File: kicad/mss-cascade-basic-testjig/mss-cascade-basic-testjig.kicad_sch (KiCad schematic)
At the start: 101 parts, among them J1 PJ-202A, J11 Molex 0532610471, J12 Molex 0532610471, J2 SM04B-SRSS, J3 SM04B-SRSS, J4 SM04B-SRSS, J5 8P8C, J6 8P8C, Q1 ZXMS6004FF, Q10 ZXMS6004FF, Q11 ZXMS6004FF, Q12 ZXMS6004FF, Q2 ZXMS6004FF, Q3 ZXMS6004FF, Q4 ZXMS6004FF, Q5 ZXMS6004FF, Q6 ZXMS6004FF, Q7 ZXMS6004FF, Q8 ZXMS6004FF, Q9 ZXMS6004FF, SW1 FSM4JSMATR, SW2 FSM4JSMATR, U1 AP7381-50, U11 PCA9555PW, U2 DRV8872DDA, U3 74HC4049, U4 INA219AxD, U5 ProMicro

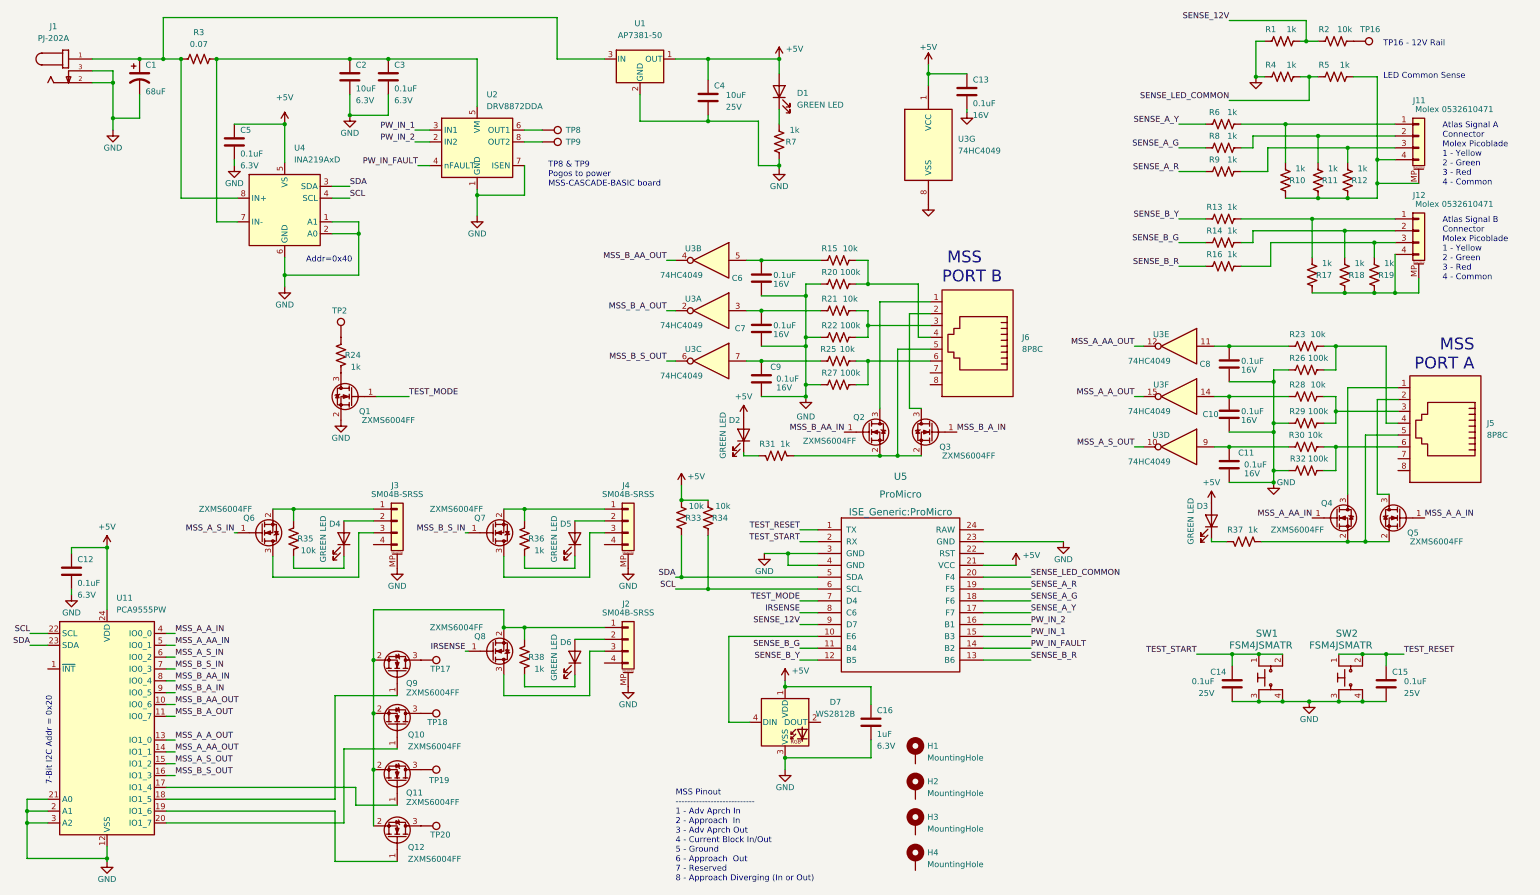
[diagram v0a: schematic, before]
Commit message: Fix issues with wire naming
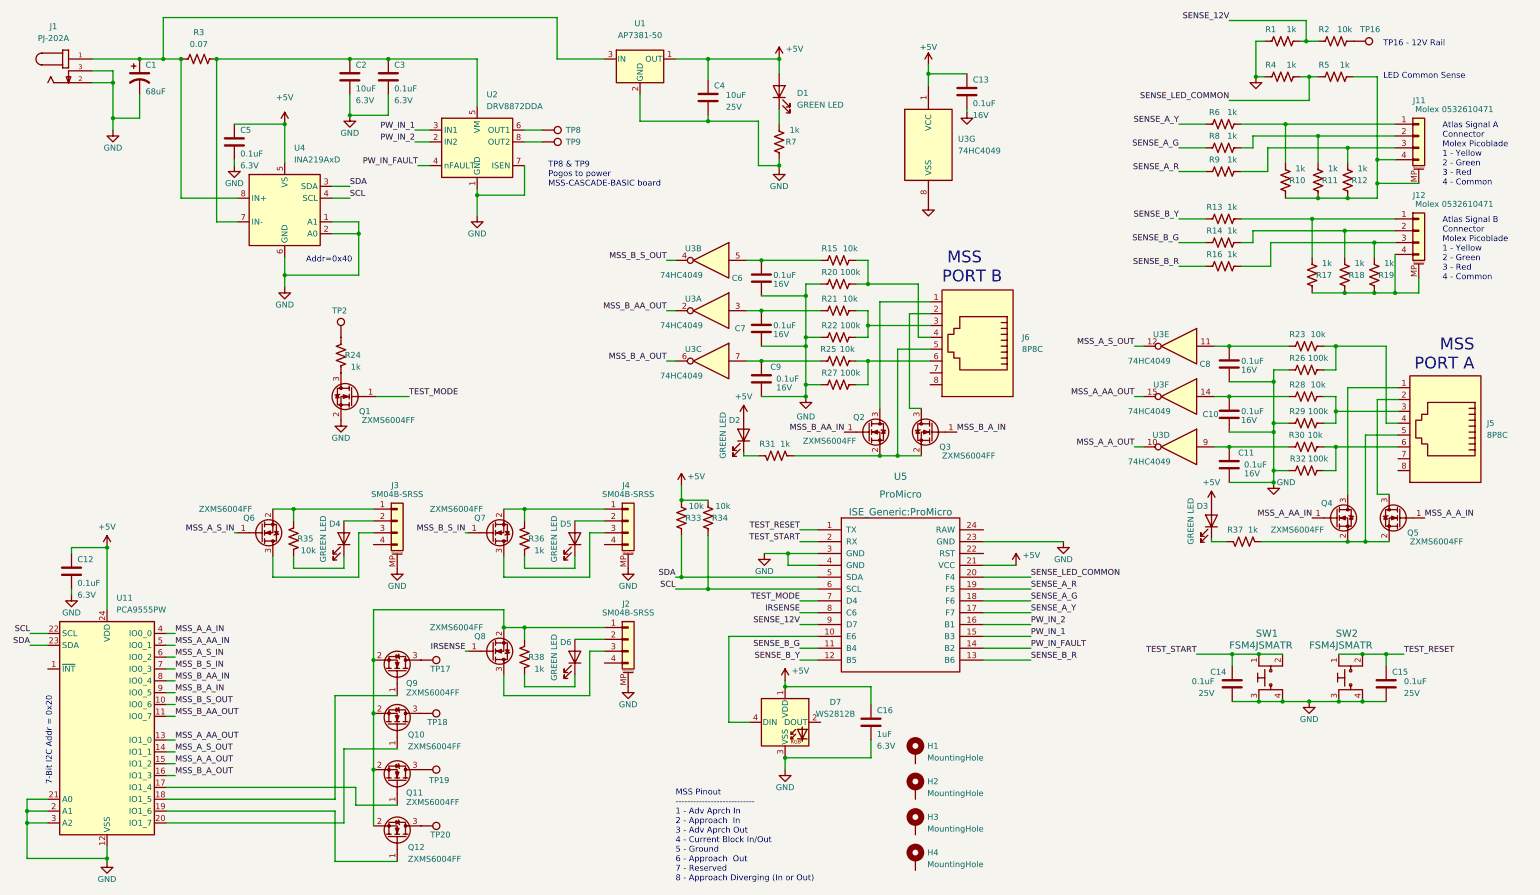
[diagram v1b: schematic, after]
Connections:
- net MSS_A_AA_OUT: now also U11.13 (IO1_0), U3.15; no longer U11.14 (IO1_1), U3.12
- net MSS_A_A_OUT: now also U11.15 (IO1_2), U3.10; no longer U11.13 (IO1_0), U3.15
- net MSS_A_S_OUT: now also U11.14 (IO1_1), U3.12; no longer U11.15 (IO1_2), U3.10
- net MSS_B_AA_OUT: now also U11.11 (IO0_7), U3.2; no longer U11.10 (IO0_6), U3.4
- net MSS_B_A_OUT: now also U11.16 (IO1_3), U3.6; no longer U11.11 (IO0_7), U3.2
- net MSS_B_S_OUT: now also U11.10 (IO0_6), U3.4; no longer U11.16 (IO1_3), U3.6
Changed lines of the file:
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@@
     (effects (font (size 1.27 1.27)) (justify right bottom))
   )
-  (label "MSS_B_A_OUT" (at 54.61 165.735 0)
+  (label "MSS_B_AA_OUT" (at 54.61 165.735 0)
     (effects (font (size 1.27 1.27)) (justify left bottom))
   )
@@
     (effects (font (size 1.27 1.27)) (justify right bottom))
   )
-  (label "MSS_B_A_OUT" (at 160.02 78.74 180)
+  (label "MSS_B_AA_OUT" (at 160.02 78.74 180)
     (effects (font (size 1.27 1.27)) (justify right bottom))
   )
-  (label "MSS_A_S_OUT" (at 260.35 107.95 180)
+  (label "MSS_A_A_OUT" (at 260.35 107.95 180)
     (effects (font (size 1.27 1.27)) (justify right bottom))
   )
-  (label "MSS_B_S_OUT" (at 160.02 89.535 180)
+  (label "MSS_B_A_OUT" (at 160.02 89.535 180)
     (effects (font (size 1.27 1.27)) (justify right bottom))
   )
@@
     (effects (font (size 1.27 1.27)) (justify left bottom))
   )
-  (label "MSS_B_S_OUT" (at 54.61 178.435 0)
+  (label "MSS_B_A_OUT" (at 54.61 178.435 0)
     (effects (font (size 1.27 1.27)) (justify left bottom))
   )
@@
     (effects (font (size 1.27 1.27)) (justify right bottom))
   )
-  (label "MSS_A_A_OUT" (at 260.35 97.155 180)
+  (label "MSS_A_AA_OUT" (at 260.35 97.155 180)
     (effects (font (size 1.27 1.27)) (justify right bottom))
   )
-  (label "MSS_A_S_OUT" (at 54.61 175.895 0)
+  (label "MSS_A_A_OUT" (at 54.61 175.895 0)
     (effects (font (size 1.27 1.27)) (justify left bottom))
   )
@@
     (effects (font (size 1.27 1.27)) (justify right bottom))
   )
-  (label "MSS_B_AA_OUT" (at 54.61 163.195 0)
+  (label "MSS_B_S_OUT" (at 54.61 163.195 0)
     (effects (font (size 1.27 1.27)) (justify left bottom))
   )
@@
     (effects (font (size 1.27 1.27)) (justify left bottom))
   )
-  (label "MSS_B_AA_OUT" (at 160.02 67.945 180)
+  (label "MSS_B_S_OUT" (at 160.02 67.945 180)
     (effects (font (size 1.27 1.27)) (justify right bottom))
   )
@@
     (effects (font (size 1.27 1.27)) (justify left bottom))
   )
-  (label "MSS_A_AA_OUT" (at 54.61 173.355 0)
+  (label "MSS_A_S_OUT" (at 54.61 173.355 0)
     (effects (font (size 1.27 1.27)) (justify left bottom))
   )
@@
     (effects (font (size 1.27 1.27)) (justify left bottom))
   )
-  (label "MSS_A_AA_OUT" (at 260.35 86.36 180)
+  (label "MSS_A_S_OUT" (at 260.35 86.36 180)
     (effects (font (size 1.27 1.27)) (justify right bottom))
   )
@@
     (effects (font (size 1.27 1.27)) (justify right bottom))
   )
-  (label "MSS_A_A_OUT" (at 54.61 170.815 0)
+  (label "MSS_A_AA_OUT" (at 54.61 170.815 0)
     (effects (font (size 1.27 1.27)) (justify left bottom))
   )
